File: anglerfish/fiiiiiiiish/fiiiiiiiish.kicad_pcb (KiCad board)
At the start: 2 copper layers, 48.9 x 35.3 mm, 3 parts

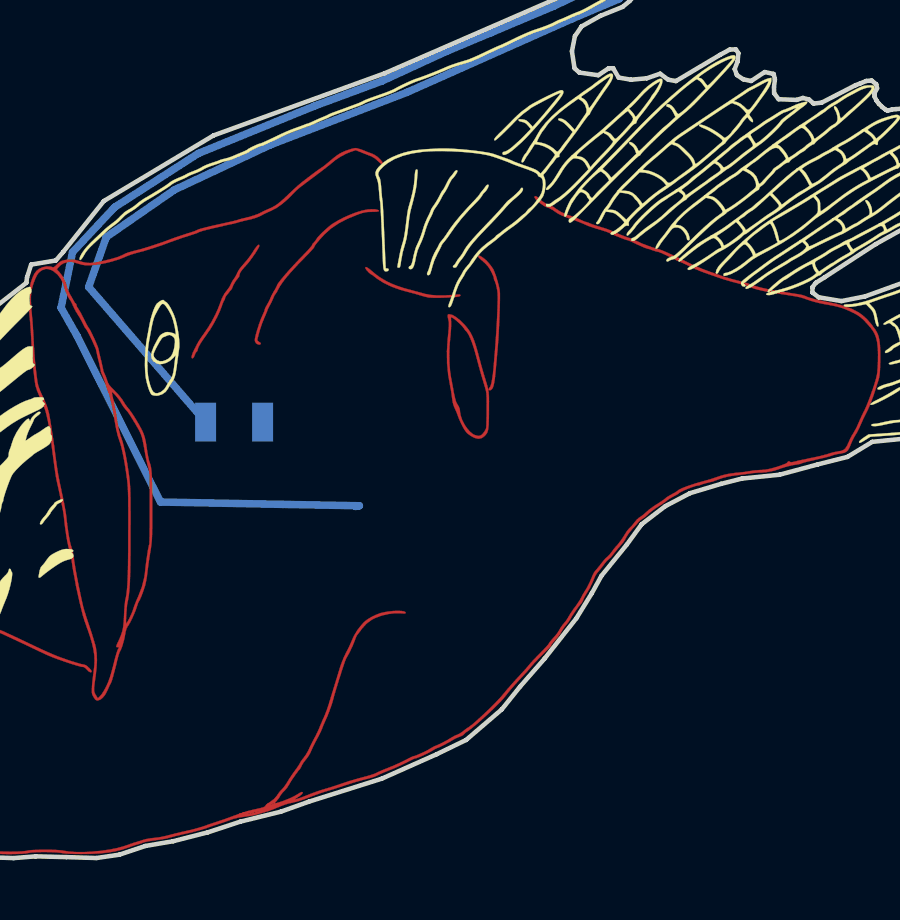
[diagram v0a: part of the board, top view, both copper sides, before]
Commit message: added power supply pads
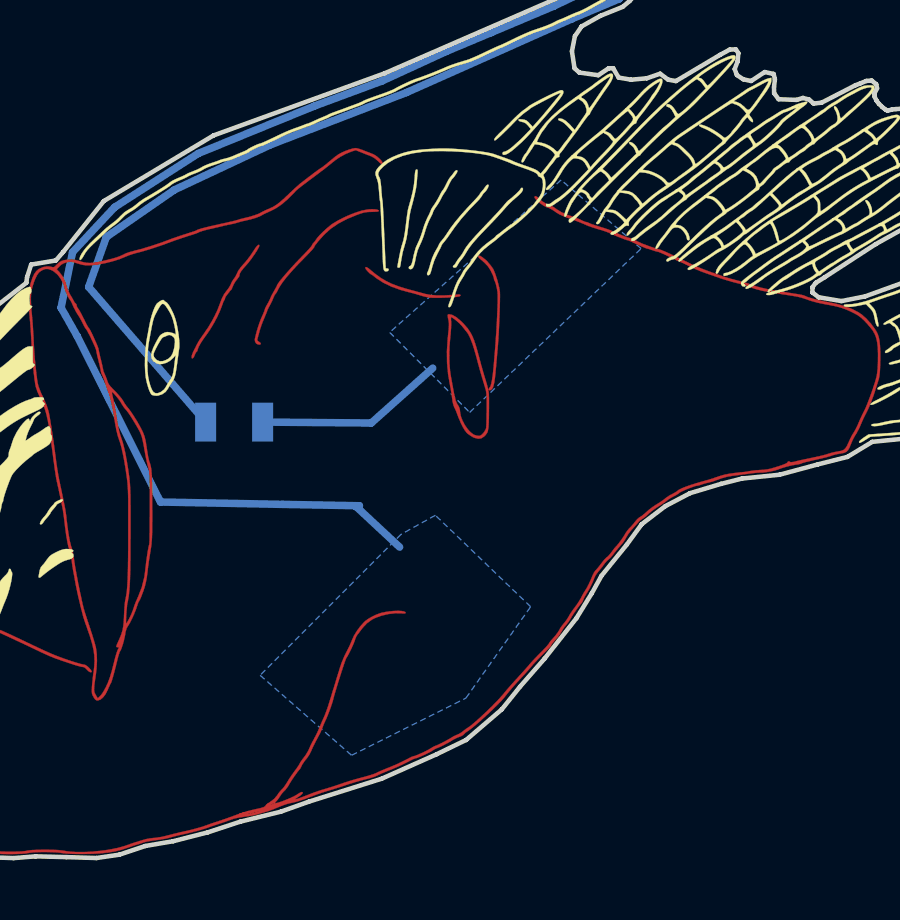
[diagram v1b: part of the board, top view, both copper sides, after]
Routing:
- net (no net): track 72.3 -> 0.00 mm
- net Net-(D1-Pad1): track 7.72 -> 68.6 mm
- net Net-(D1-Pad2): track 60.8 -> 74.3 mm
- net Net-(R1-Pad2): track 0.00 -> 6.37 mm
- added copper zone on B.Cu, net Net-(D1-Pad2)
- added copper zone on B.Cu, net Net-(R1-Pad2)

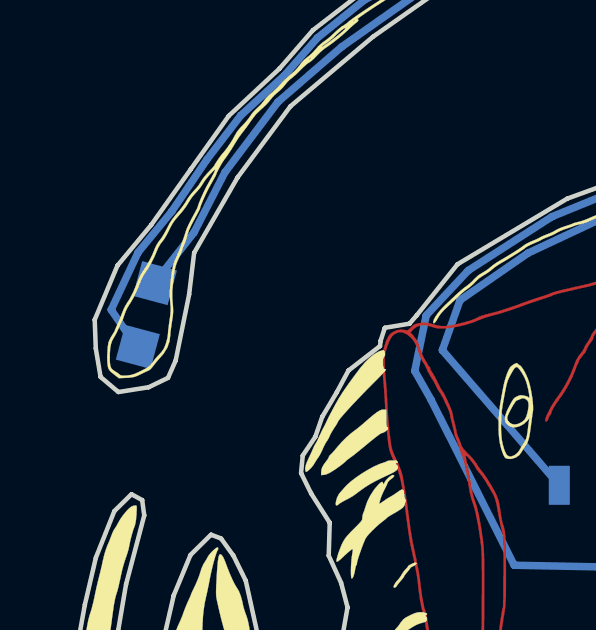
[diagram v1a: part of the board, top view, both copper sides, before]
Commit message: changed to circle reliefed led
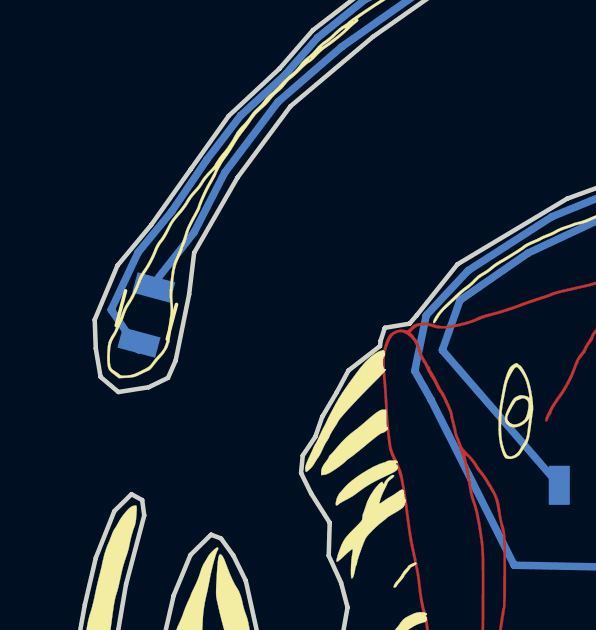
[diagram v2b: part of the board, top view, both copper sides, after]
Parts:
- D1: footprint LEDs:LED_0805 -> SillyComps:GlowBug_CircleRelief; moved to F.Cu
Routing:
- net (no net): track 0.00 -> 74.3 mm
- net Net-(D1-Pad1): track 68.6 -> 5.96 mm
- net Net-(D1-Pad2): track 74.3 -> 62.6 mm

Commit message: updated bottom pad
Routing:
- net (no net): track 74.3 -> 0.00 mm
- net Net-(D1-Pad1): track 5.96 -> 68.6 mm
- net Net-(D1-Pad2): track 62.6 -> 74.3 mm
